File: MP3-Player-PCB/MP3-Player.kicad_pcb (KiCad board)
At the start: 4 copper layers, 50 x 50 mm, 113 parts, among them J101 Conn_ARM_SWD_TagConnect_TC2030, J201 Conn_01x02_Socket, J202 USB_C_Receptacle_USB2.0_16P, J301 Micro_SD_Card_Det1, Q301 AO3401A, Q302 2N7002H, Q303 AO3401A, Q304 AO3401A, Q305 2N7002H, SW301 1-1825910-4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

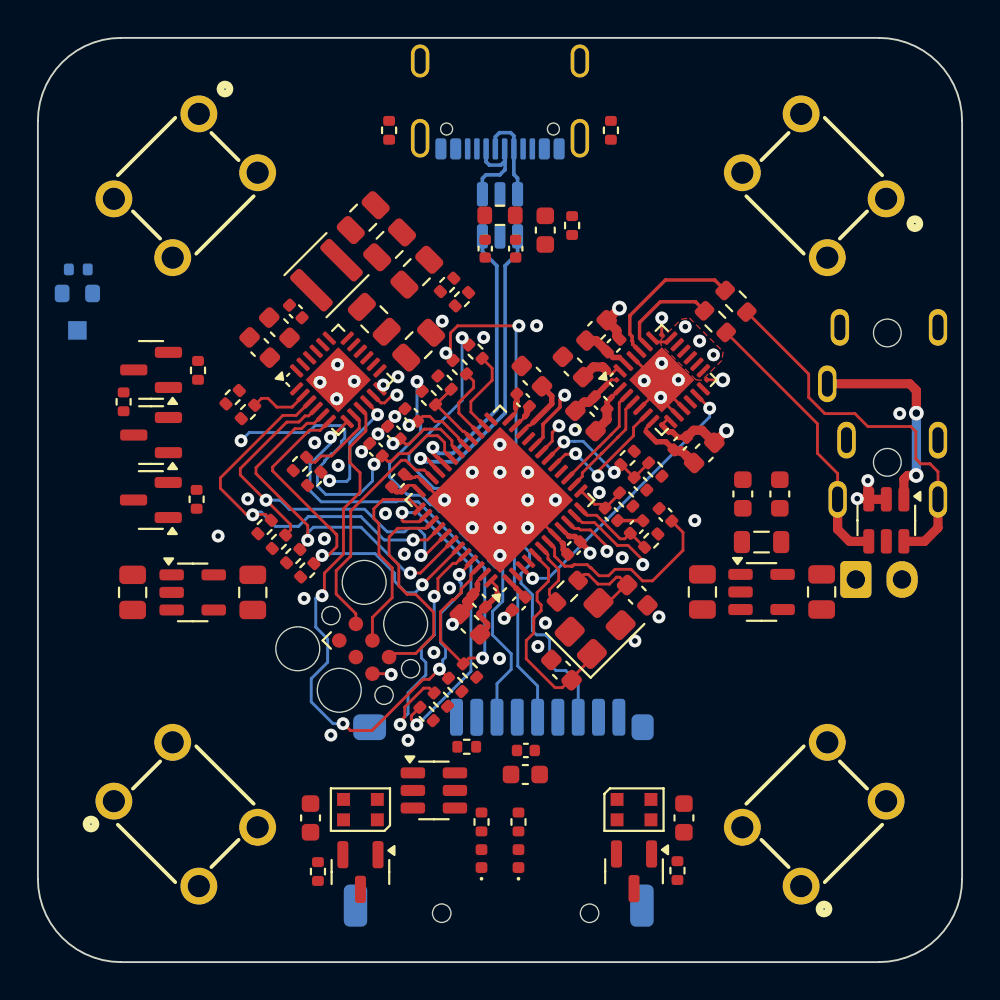
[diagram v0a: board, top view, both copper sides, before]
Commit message: Finished SD card routing
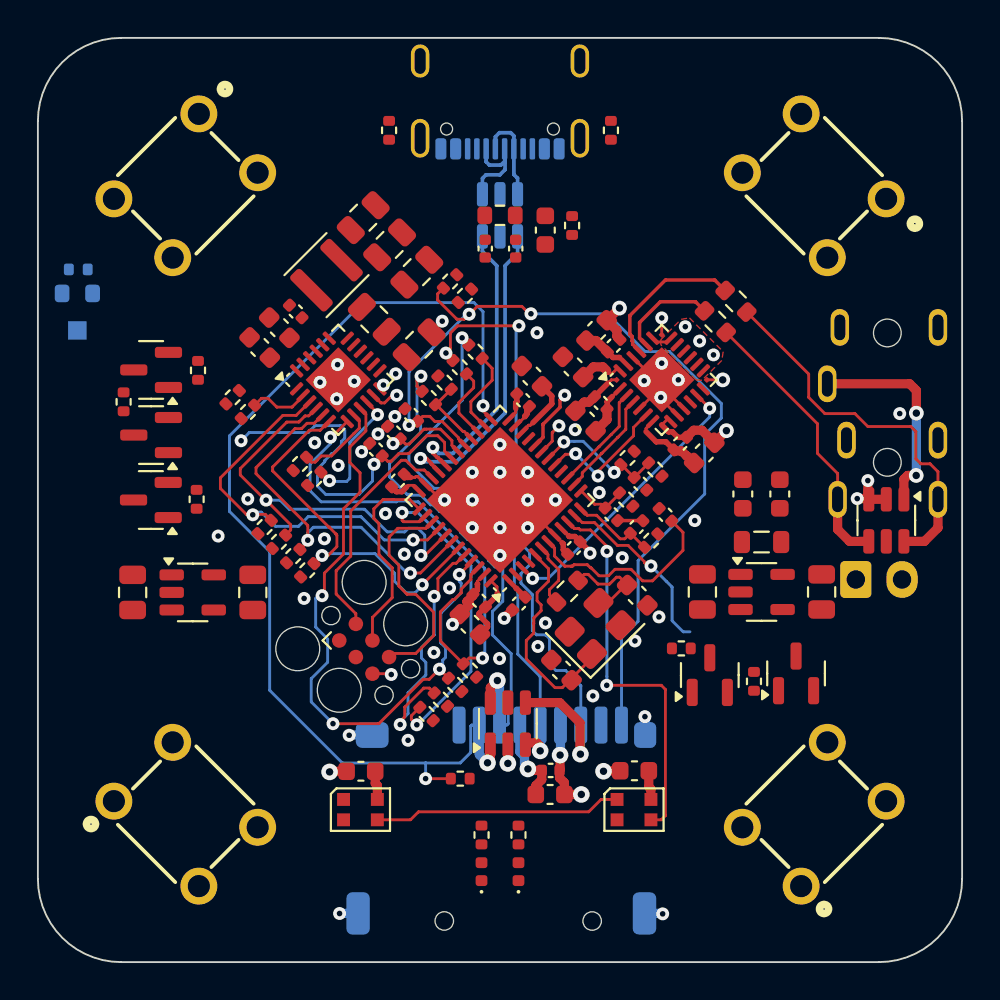
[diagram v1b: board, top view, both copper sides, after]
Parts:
- moved Q302 25.9 mm to (141.0, 134.4), turned to 90 degrees
- moved R312 25.7 mm to (138.7, 134.8)
- moved D301 14.8 mm to (132.2, 141.8), turned to 0 degrees
- moved D302 14.8 mm to (117.5, 141.8)
- moved R311 12.0 mm to (134.8, 133.0), turned to 0 degrees
- moved Q301 11.4 mm to (136.3, 134.5), turned to 90 degrees
- moved U301 5.39 mm to (125.4, 137.1), turned to 90 degrees
- moved C305 3.72 mm to (117.5, 139.7), turned to 180 degrees
- moved C304 3.70 mm to (132.3, 139.7), turned to 180 degrees
- moved R301 1.76 mm to (122.8, 140.1), turned to 180 degrees
- moved C301 1.72 mm to (127.7, 140.9)
- moved C302 1.72 mm to (127.7, 139.6)
- moved R103 0.71 mm to (126.0, 143.1)
- moved R104 0.71 mm to (124.0, 143.1)
- moved D101 0.70 mm to (126.0, 145.1)
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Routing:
- net SD_CARD_NCS: track 0.00 -> 57.7 mm, vias 0 -> 3
- net SD_CARD_NCD: track 3.91 -> 50.0 mm, vias 1 -> 3
- net LEDS_TIM2_PWM: track 2.93 -> 21.2 mm, vias 1 -> 2
- net /Peripherals/RGB1_RGB2: track 0.00 -> 13.4 mm
- net GND: track 41.5 -> 53.4 mm, vias 61 -> 69
- net /Peripherals/SD_CARD_MISO_PIN: track 28.7 -> 35.9 mm, vias 2 -> 3
- net /Peripherals/SD_CARD_MOSI_PIN: track 24.0 -> 29.2 mm, vias 1 -> 2
- net LEDS_PWR_EN: track 5.03 -> 9.96 mm
- net +3.3V: track 14.1 -> 18.9 mm, vias 1 -> 2
- net +VSYS_LED: track 0.00 -> 3.17 mm
- net /Peripherals/SD_CARD_SCK_PIN: track 25.7 -> 28.7 mm, vias 1 -> 2

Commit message: Finished RGB LED routing
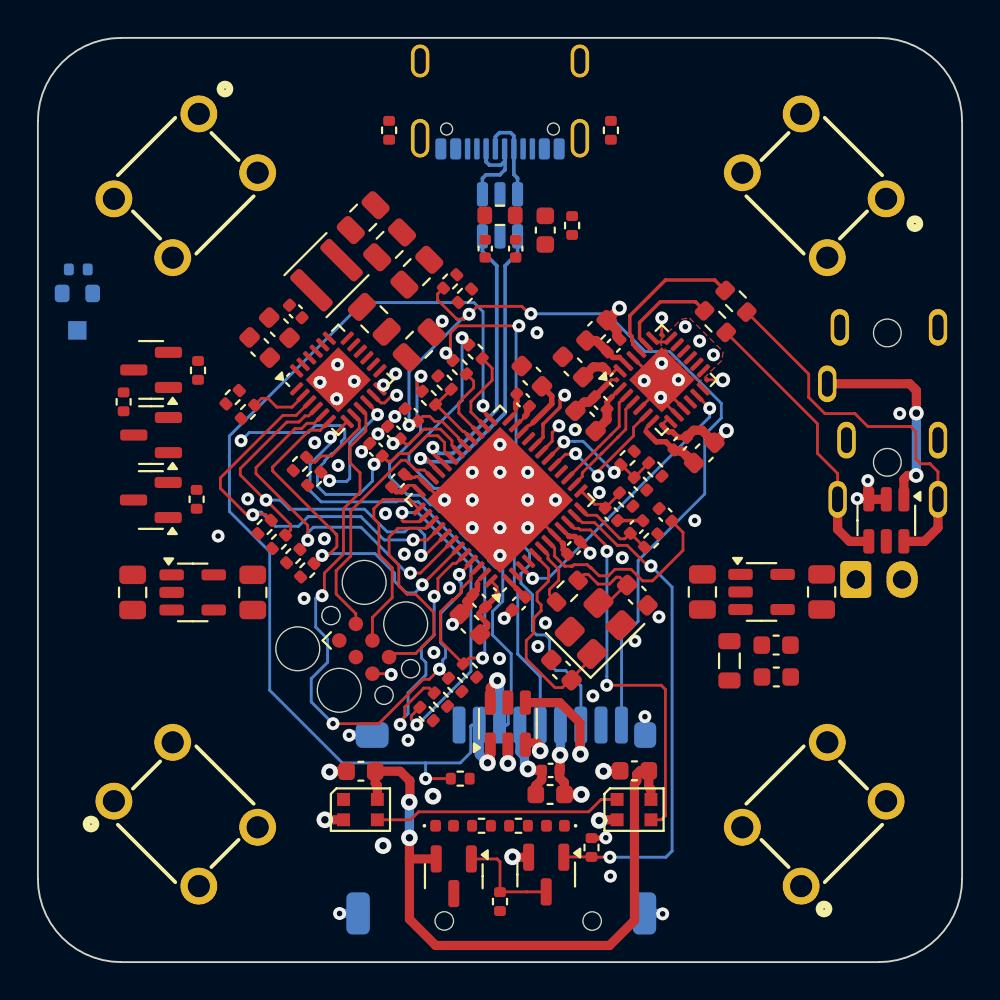
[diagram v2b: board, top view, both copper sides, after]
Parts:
- moved Q301 17.6 mm to (122.5, 145.4), turned to -90 degrees
- moved Q302 17.4 mm to (127.5, 145.3), turned to -90 degrees
- moved R311 16.8 mm to (125.0, 146.7), turned to 90 degrees
- moved R312 12.6 mm to (129.9, 143.8)
- moved C212 9.90 mm to (139.9, 134.6), turned to 0 degrees
- moved C213 8.37 mm to (139.9, 132.8), turned to 0 degrees
- moved FB201 6.66 mm to (137.4, 133.7), turned to 90 degrees
- moved D101 3.19 mm to (128.0, 142.6), turned to 180 degrees
- moved D102 3.19 mm to (122.0, 142.6), turned to 0 degrees
- moved R103 0.50 mm to (126.0, 142.6), turned to 0 degrees
- moved R104 0.50 mm to (124.0, 142.6), turned to 180 degrees
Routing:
- net +VSYS_LED: track 3.17 -> 36.3 mm, vias 0 -> 2
- net LEDS_PWR_EN: track 9.96 -> 27.2 mm, vias 1 -> 2
- net /Peripherals/LED_GATE: track 0.00 -> 5.72 mm
- net GND: track 53.4 -> 57.1 mm, vias 69 -> 76

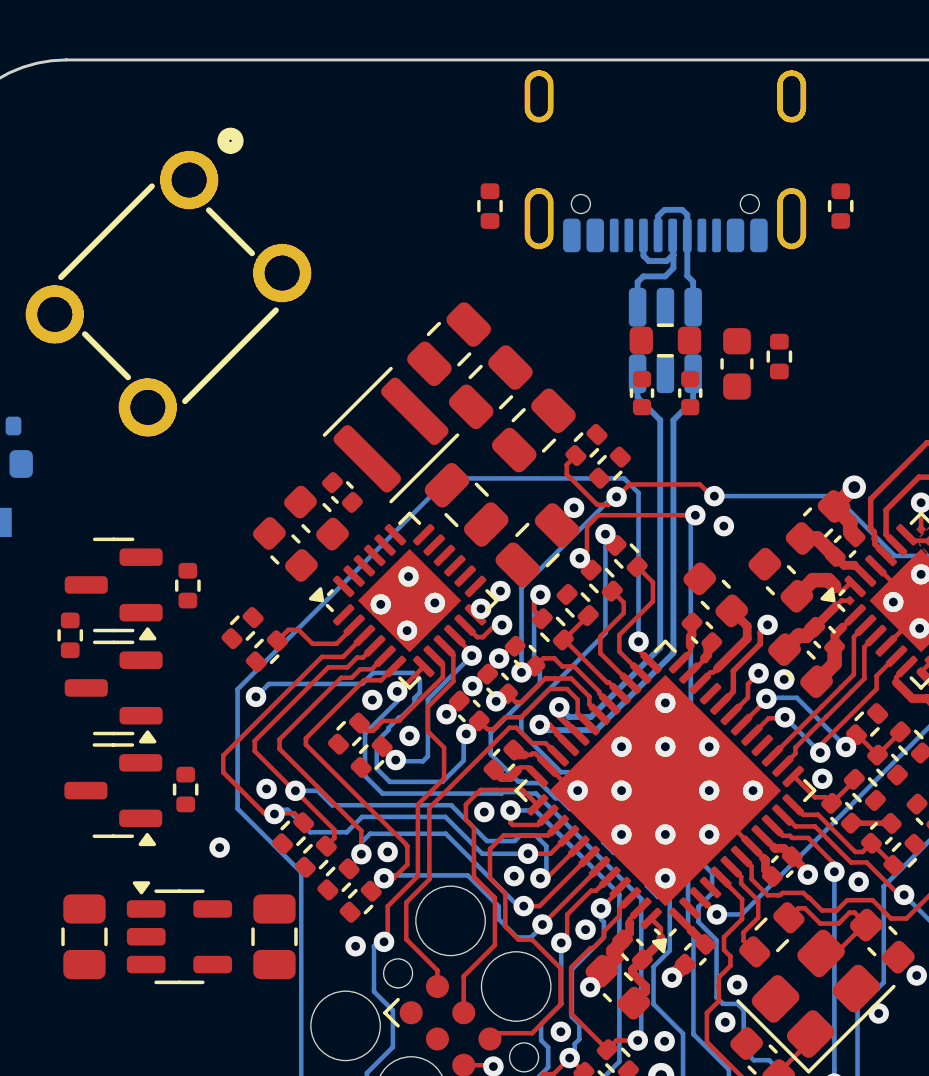
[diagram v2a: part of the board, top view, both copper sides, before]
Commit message: Completed much of the USB-C charging IC power routing
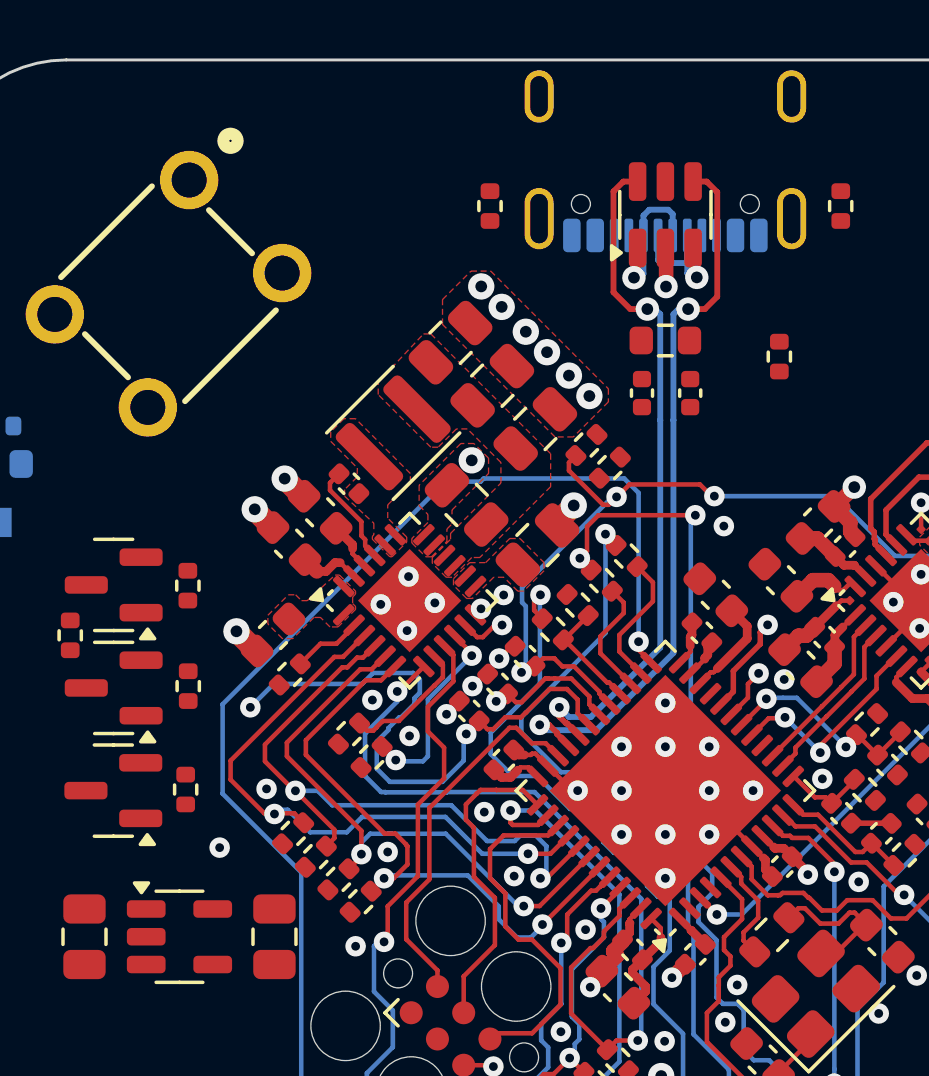
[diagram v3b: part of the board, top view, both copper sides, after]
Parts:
- U202: moved to F.Cu
- moved C203 18.4 mm to (111.6, 119.7), turned to -135 degrees
- moved U202 4.30 mm to (125.0, 105.3), turned to 90 degrees
- moved R309 2.72 mm to (108.7, 121.4), turned to -90 degrees
- moved R204 1.11 mm to (112.2, 121.0)
- moved C204 0.37 mm to (114.2, 114.5), turned to -45 degrees
- moved C209 0.24 mm to (112.1, 116.5)
- moved C211 0.24 mm to (113.2, 115.5)
- moved L201 0.11 mm to (115.7, 112.8)
- moved C207 0.07 mm to (117.7, 109.7)
- moved C208 0.07 mm to (119.1, 111.1)
- moved C206 0.07 mm to (120.5, 112.6)
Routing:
- net USB_MCU_D+: track 17.1 -> 25.2 mm, vias 1 -> 2
- net USB_MCU_D-: track 15.5 -> 23.6 mm, vias 1 -> 2
- net GND: track 57.1 -> 62.1 mm, vias 76 -> 87
- net /Power/BAT_BTST: track 0.00 -> 3.56 mm
- net /Power/BAT_PMID: track 0.00 -> 2.16 mm
- net /Power/BAT_REGN: track 0.00 -> 1.68 mm
- net /Power/BAT_PSEL: track 3.28 -> 2.42 mm
- net BAT_STAT: track 22.8 -> 22.3 mm
- net /Power/USB_CON_D+: track 5.06 -> 5.62 mm, vias 0 -> 1
- net /Power/USB_CON_D-: track 5.36 -> 5.31 mm, vias 0 -> 1
- added copper zone on F.Cu, net +VBAT
- added copper zone on F.Cu, net +VSYS
- added copper zone on F.Cu, net +VUSB_FILT
- added copper zone on F.Cu, net /Power/BAT_SW

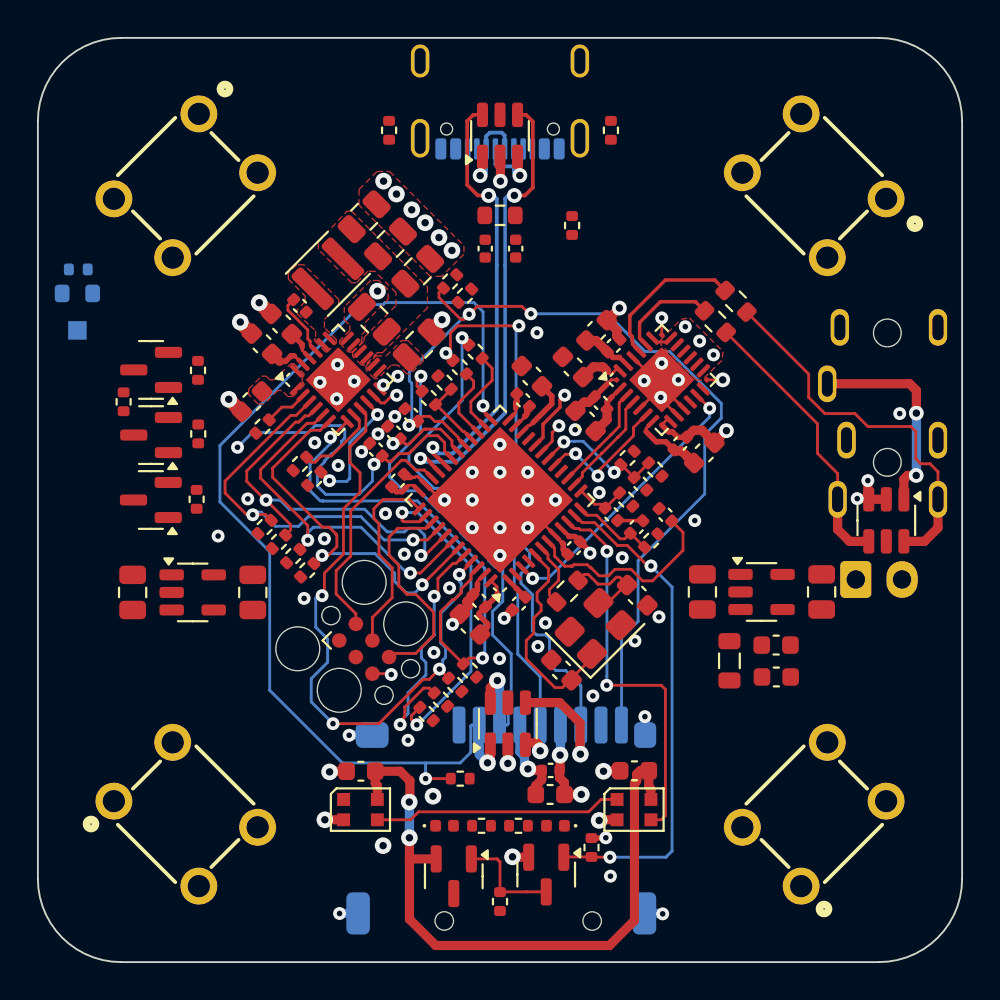
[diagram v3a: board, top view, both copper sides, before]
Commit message: Routed button gpio signals
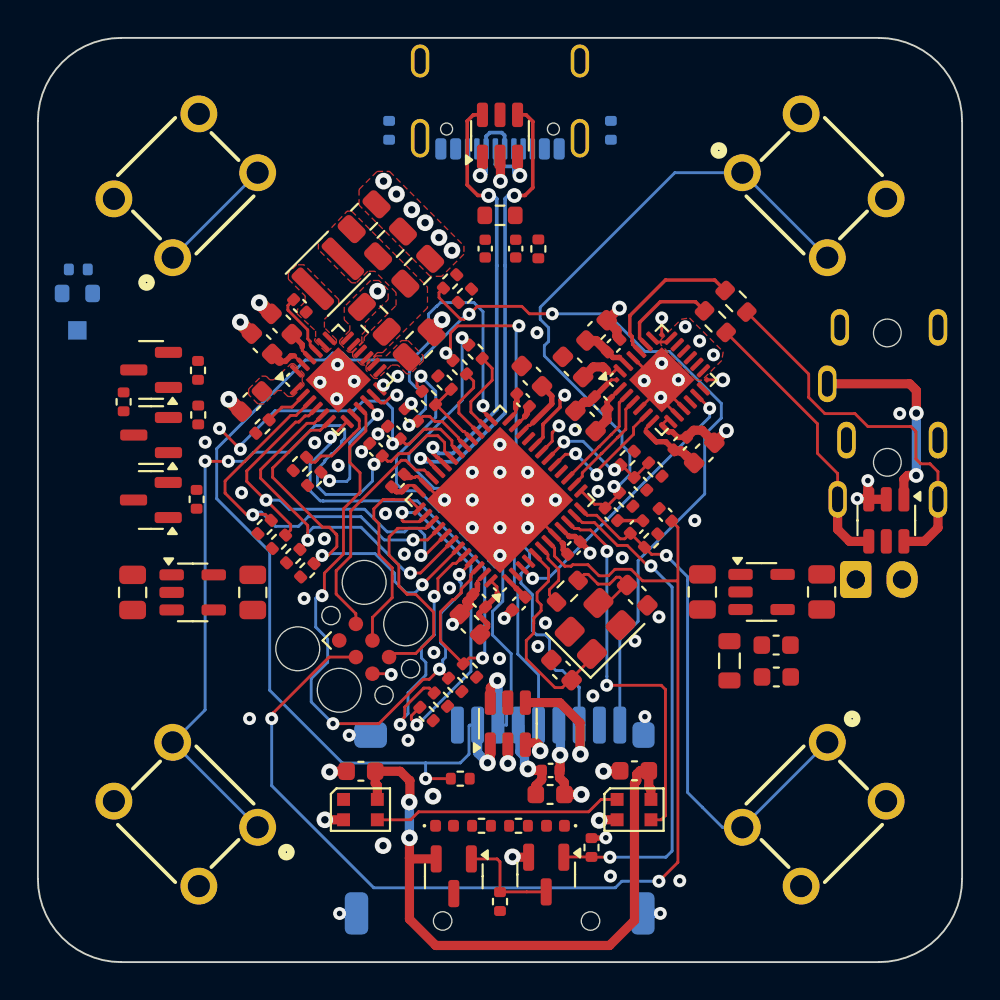
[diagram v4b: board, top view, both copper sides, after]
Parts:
- R205, R206: moved to B.Cu
- moved SW302 48.1 mm to (142.0, 108.0)
- moved SW303 48.1 mm to (108.0, 142.0)
- moved R202 2.22 mm to (127.1, 111.4)
- moved R309 1.02 mm to (108.7, 120.4)
- moved J301 0.09 mm to (125.0, 142.3)
- turned SW301 to -135 degrees
- turned SW304 to 45 degrees
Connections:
- C110 pad 1: BUTTON_3 -> BUTTON_4
- C111 pad 1: BUTTON_4 -> BUTTON_3
- U101 pad 30: BUTTON_3 -> BUTTON_4
- U101 pad 31: BUTTON_4 -> BUTTON_3
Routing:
- net /MCU/NRST: track 11.3 -> 61.6 mm, vias 0 -> 2
- net BUTTON_3: track 4.77 -> 44.9 mm, vias 1 -> 3
- net BUTTON_2: track 2.84 -> 36.2 mm, vias 0 -> 1
- net BUTTON_1: track 4.56 -> 29.5 mm, vias 0 -> 1
- net /Peripherals/BUTTON4_GATE: track 0.00 -> 6.50 mm
- net BUTTON_4: track 20.4 -> 17.9 mm, vias 2 -> 3
- net SD_CARD_NCS: track 58.2 -> 59.5 mm
- net SD_CARD_NCD: track 49.9 -> 50.7 mm
- net GND: track 62.1 -> 61.8 mm, vias 87 -> 89

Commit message: Finished USB power routing
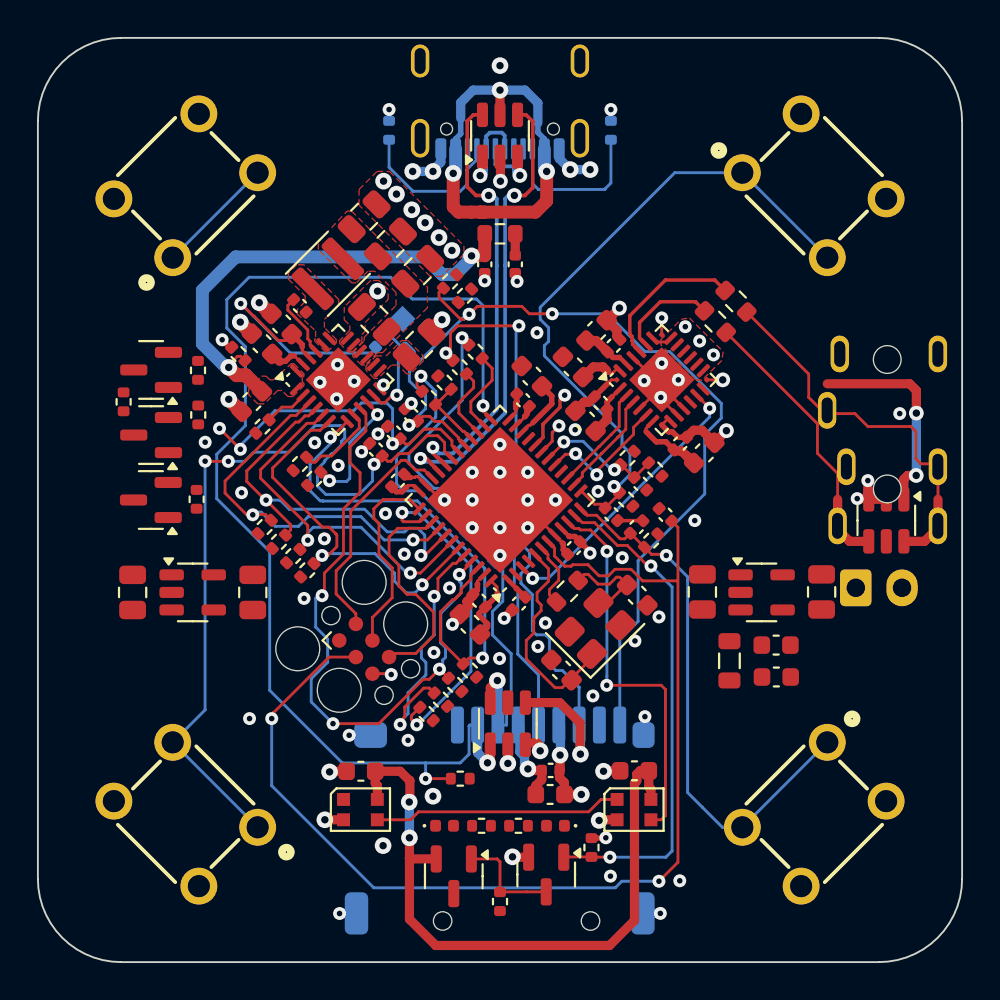
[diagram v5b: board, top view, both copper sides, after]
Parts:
- moved TH201 18.5 mm to (120.5, 116.4), turned to 45 degrees
- moved TP201 17.6 mm to (119.7, 115.2), turned to 45 degrees
- moved R202 17.2 mm to (110.8, 117.1), turned to -45 degrees
- moved R207 16.9 mm to (118.6, 116.4), turned to 45 degrees
- moved C202 1.88 mm to (124.2, 112.2)
- moved C201 1.83 mm to (125.8, 112.2)
- moved U402 1.44 mm to (145.7, 121.8)
- moved R201 1.00 mm to (125.0, 110.6), turned to 180 degrees
- moved J201 0.45 mm to (144.2, 129.8)
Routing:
- net +VUSB_FILT: track 0.00 -> 26.8 mm, vias 0 -> 2
- net +VUSB: track 0.00 -> 24.2 mm, vias 0 -> 3
- net /Power/BAT_REGN: track 1.68 -> 14.0 mm, vias 0 -> 1
- net /Power/USB_CON_CC2: track 0.00 -> 8.75 mm
- net /Power/USB_CON_CC1: track 0.00 -> 8.55 mm
- net GND: track 61.8 -> 69.6 mm, vias 89 -> 98
- net SD_CARD_NCS: track 59.5 -> 64.9 mm
- net /Power/BAT_TS: track 1.65 -> 6.69 mm
